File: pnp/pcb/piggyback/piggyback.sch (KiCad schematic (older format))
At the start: 14 parts, among them J37 Screw_Terminal_01x03, J38 AVR-ISP-6, J39 SERIAL_INTERFACE, J4 USB_B_Micro, U2 ATmega32U4-AU, Y1 16MHz

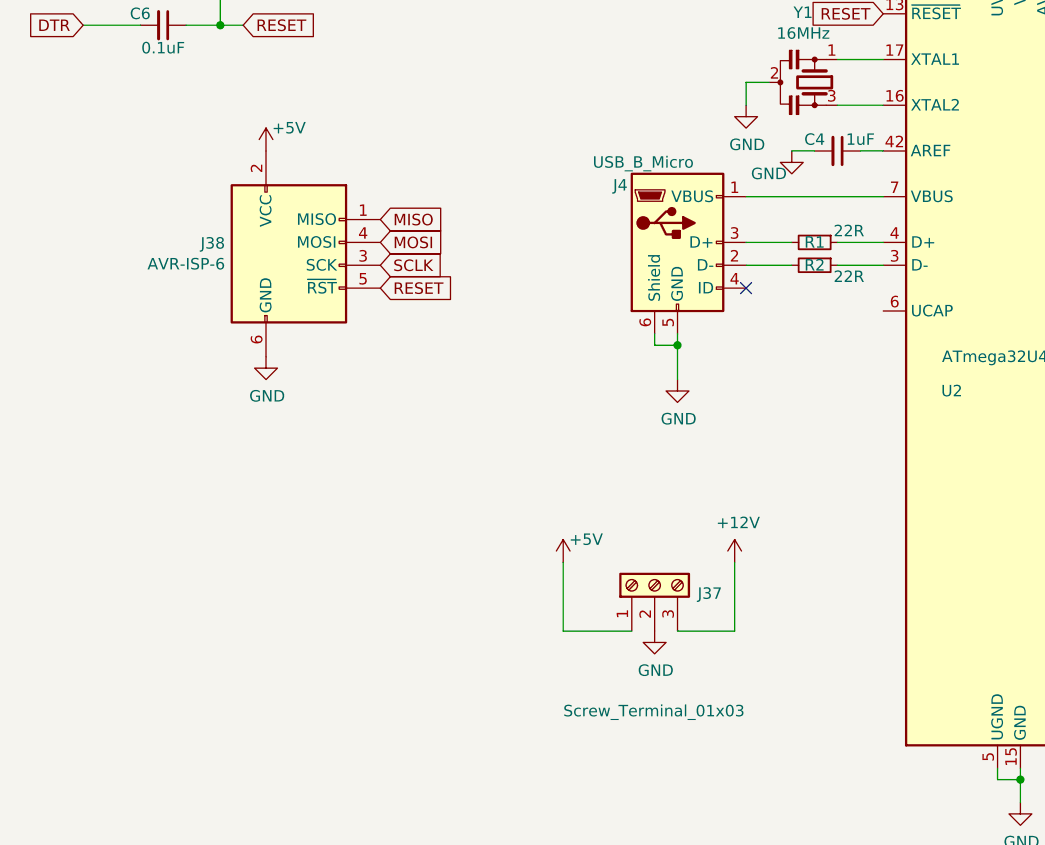
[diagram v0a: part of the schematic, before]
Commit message: Adding feeder and pnp CAD, updating Piggyback to fix USB, MCP23017 Reset pullup, and add uC reset button.
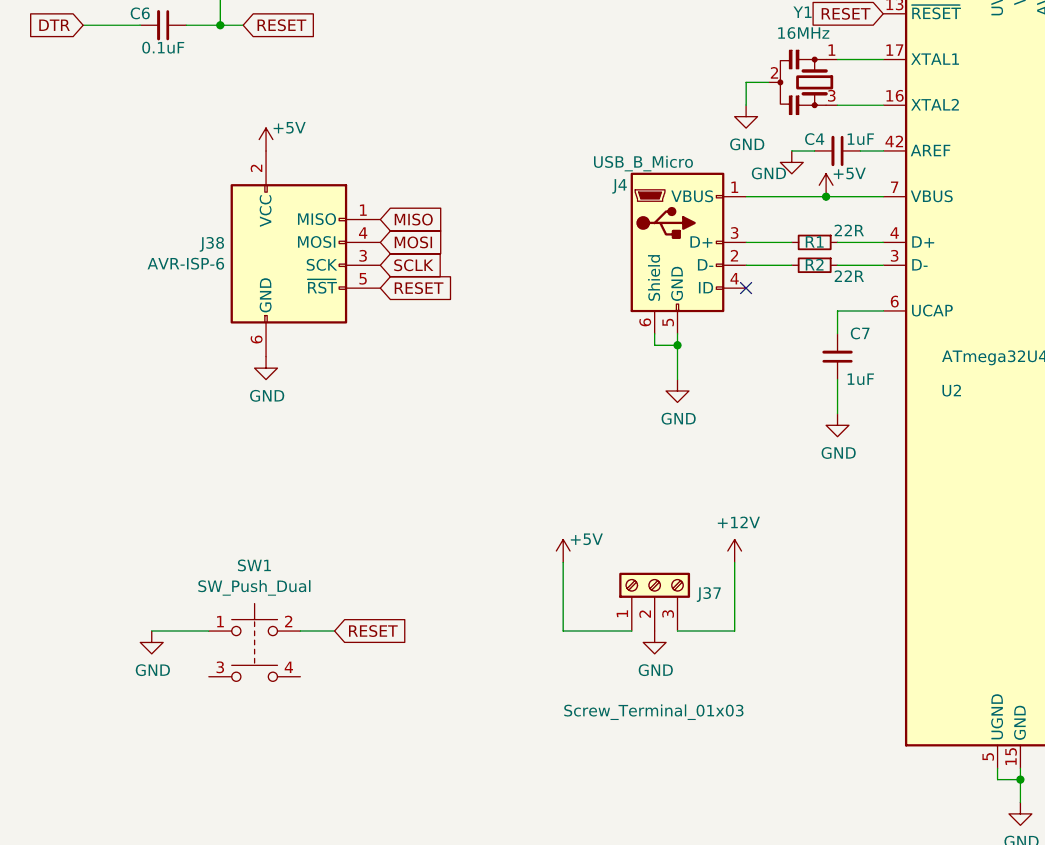
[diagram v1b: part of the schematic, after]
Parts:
- added C7: 1uF, Capacitor_SMD:C_0805_2012Metric_Pad1.15x1.40mm_HandSolder, symbol Device:C_Small
- added SW1: SW_Push_Dual, Button_Switch_SMD:SW_SPST_B3S-1000, symbol Switch:SW_Push_Dual
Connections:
- net +5V: now also J4.1 (VBUS), U2.7 (VBUS)
- net GND: now also C7.1, SW1.1
- net RESET: now also SW1.2
- net at U2.6 (UCAP): now also C7.2
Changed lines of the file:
@@
 	4500 3150 4300 3150
 Wire Wire Line
-	4300 2950 4900 2950
+	4300 2950 4650 2950
 $Comp
 L power:GND #PWR0113
@@
 	0    -1   -1   0
 $EndComp
+$Comp
+L power:GND #PWR0212
+U 1 1 5EA5D10C
+P 4700 3900
+F 0 "#PWR0212" H 4700 3650 50  0001 C CNN
+F 1 "GND" H 4705 3727 50  0000 C CNN
+F 2 "" H 4700 3900 50  0001 C CNN
+F 3 "" H 4700 3900 50  0001 C CNN
+	1    4700 3900
+	1    0    0    -1
+$EndComp
+$Comp
+L Device:C_Small C7
+U 1 1 5EA5D5C9
+P 4700 3650
+F 0 "C7" H 4600 3550 50  0000 C CNN
+F 1 "1uF" H 4600 3750 50  0000 C CNN
+F 2 "Capacitor_SMD:C_0805_2012Metric_Pad1.15x1.40mm_HandSolder" H 4700 3650 50  0001 C CNN
+F 3 "~" H 4700 3650 50  0001 C CNN
+	1    4700 3650
+	-1   0    0    1
+$EndComp
+Wire Wire Line
+	4900 3450 4700 3450
+Wire Wire Line
+	4700 3450 4700 3550
+Wire Wire Line
+	4700 3750 4700 3900
+$Comp
+L power:+5V #PWR0213
+U 1 1 5EA5FD6E
+P 4650 2950
+F 0 "#PWR0213" H 4650 2800 50  0001 C CNN
+F 1 "+5V" H 4750 3050 50  0000 C CNN
+F 2 "" H 4650 2950 50  0001 C CNN
+F 3 "" H 4650 2950 50  0001 C CNN
+	1    4650 2950
+	1    0    0    -1
+$EndComp
+Connection ~ 4650 2950
+Wire Wire Line
+	4650 2950 4900 2950
+$Comp
+L Switch:SW_Push_Dual SW1
+U 1 1 5EA610D5
+P 2150 4850
+F 0 "SW1" H 2150 5135 50  0000 C CNN
+F 1 "SW_Push_Dual" H 2150 5044 50  0000 C CNN
+F 2 "Button_Switch_SMD:SW_SPST_B3S-1000" H 2150 5050 50  0001 C CNN
+F 3 "" H 2150 5050 50  0001 C CNN
+	1    2150 4850
+	1    0    0    -1
+$EndComp
+Text GLabel 2500 4850 2    50   Input ~ 0
+RESET
+$Comp
+L power:GND #PWR0214
+U 1 1 5EA630B2
+P 1700 4850
+F 0 "#PWR0214" H 1700 4600 50  0001 C CNN
+F 1 "GND" H 1705 4677 50  0000 C CNN
+F 2 "" H 1700 4850 50  0001 C CNN
+F 3 "" H 1700 4850 50  0001 C CNN
+	1    1700 4850
+	1    0    0    -1
+$EndComp
+Wire Wire Line
+	1700 4850 1950 4850
+Wire Wire Line
+	2350 4850 2500 4850
 $EndSCHEMATC
